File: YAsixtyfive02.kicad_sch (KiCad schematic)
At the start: 60 parts, among them J1 ~{NMI}, J2 Aux 5VDC, J3 Power 5V, J4 Expansion Bus, J7 GND, J8 FTDI Serial2USB, SW1 RESET, SW2 SW_Push_DPDT, U1 WD65C02, U10 74LS138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

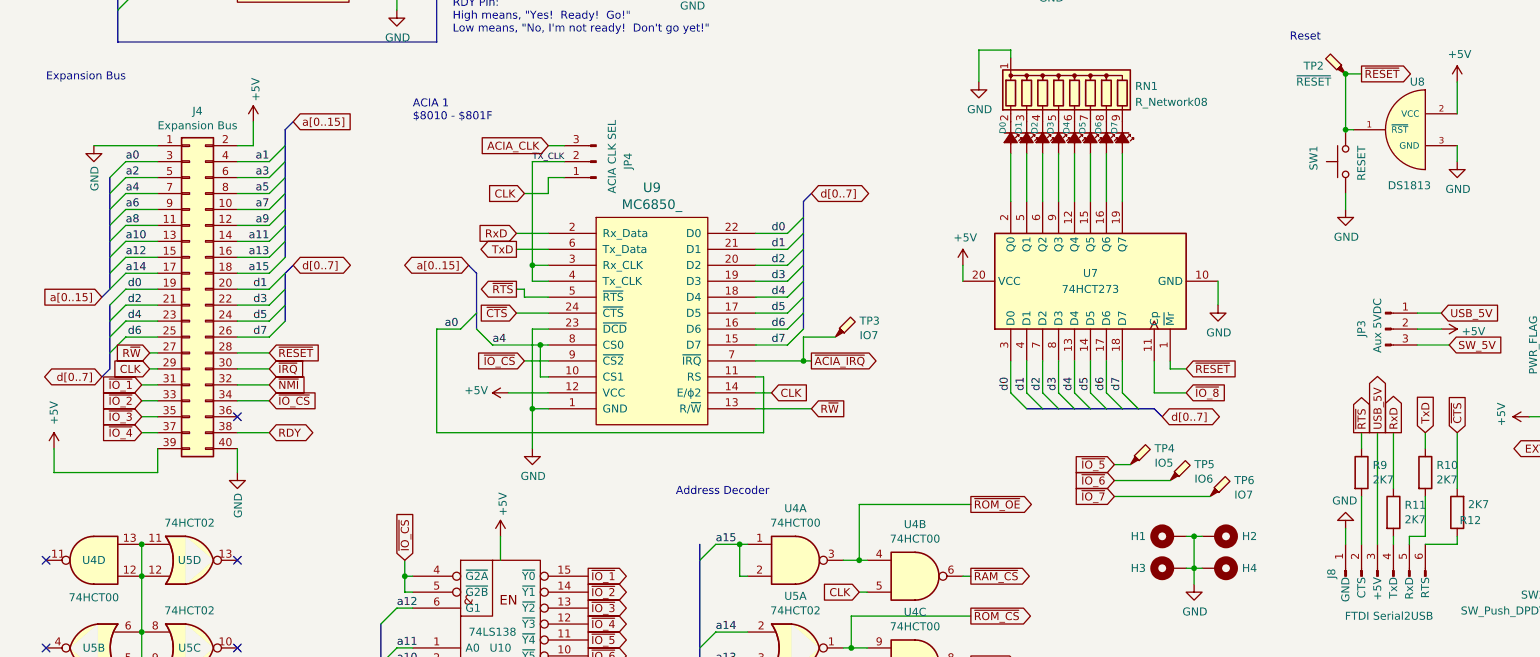
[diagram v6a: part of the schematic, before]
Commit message: PCB Almost ready missing USB Power override
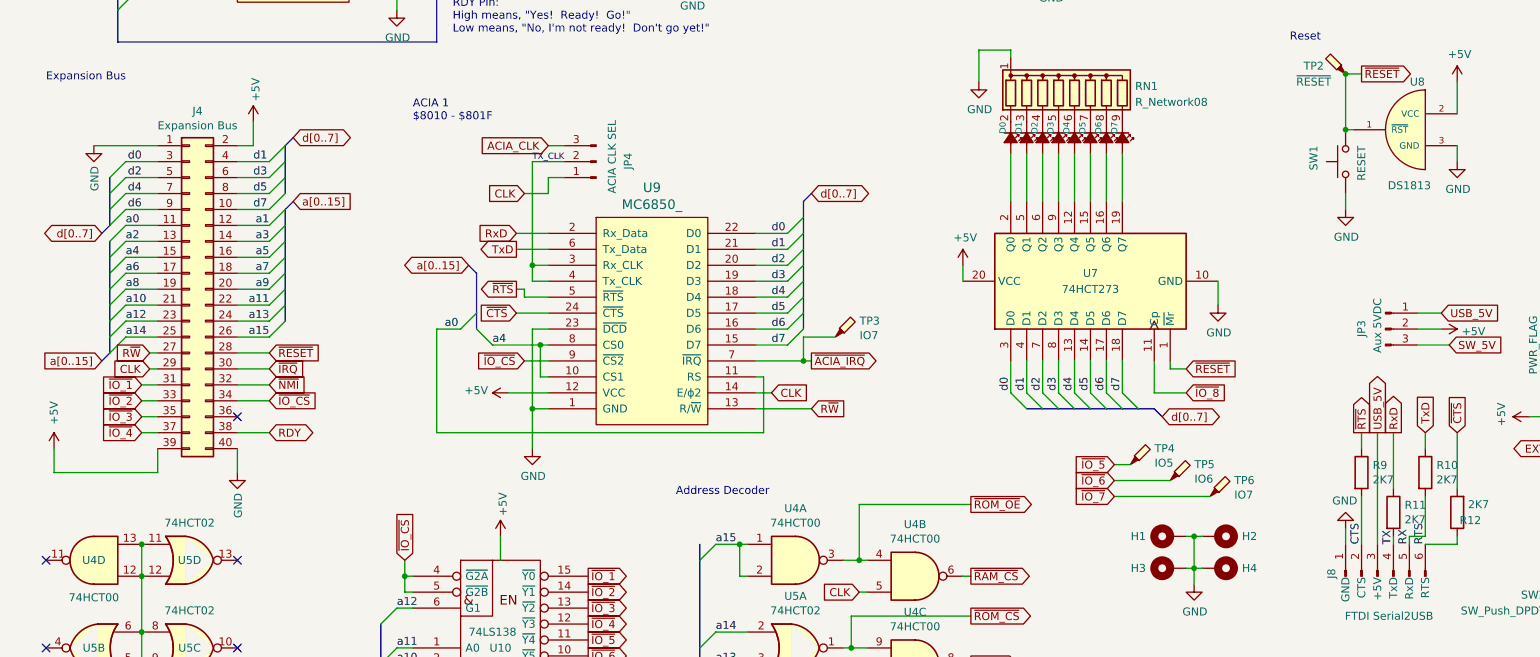
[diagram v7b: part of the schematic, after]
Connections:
- net a0: now also J4.11 (Pin_11); no longer J4.3 (Pin_3)
- net a1: now also J4.12 (Pin_12); no longer J4.4 (Pin_4)
- net a10: now also J4.21 (Pin_21); no longer J4.13 (Pin_13)
- net a11: now also J4.22 (Pin_22); no longer J4.14 (Pin_14)
- net a12: now also J4.23 (Pin_23); no longer J4.15 (Pin_15)
- net a13: now also J4.24 (Pin_24); no longer J4.16 (Pin_16)
- net a14: now also J4.25 (Pin_25); no longer J4.17 (Pin_17)
- net a15: now also J4.26 (Pin_26); no longer J4.18 (Pin_18)
- net a2: now also J4.13 (Pin_13); no longer J4.5 (Pin_5)
- net a3: now also J4.14 (Pin_14); no longer J4.6 (Pin_6)
- net a4: now also J4.15 (Pin_15); no longer J4.7 (Pin_7)
- net a5: now also J4.16 (Pin_16); no longer J4.8 (Pin_8)
- net a6: now also J4.17 (Pin_17); no longer J4.9 (Pin_9)
- net a7: now also J4.18 (Pin_18); no longer J4.10 (Pin_10)
- net a8: now also J4.19 (Pin_19); no longer J4.11 (Pin_11)
- net a9: now also J4.20 (Pin_20); no longer J4.12 (Pin_12)
- net d0: now also J4.3 (Pin_3); no longer J4.19 (Pin_19)
- net d1: now also J4.4 (Pin_4); no longer J4.20 (Pin_20)
- net d2: now also J4.5 (Pin_5); no longer J4.21 (Pin_21)
- net d3: now also J4.6 (Pin_6); no longer J4.22 (Pin_22)
- net d4: now also J4.7 (Pin_7); no longer J4.23 (Pin_23)
- net d5: now also J4.8 (Pin_8); no longer J4.24 (Pin_24)
- net d6: now also J4.9 (Pin_9); no longer J4.25 (Pin_25)
- net d7: now also J4.10 (Pin_10); no longer J4.26 (Pin_26)
- net CTS: now reaches J8.2 (CTS), R9.2
- net TX: now reaches J8.4 (TxD), R11.2
- net RX: now reaches J8.5 (RxD), R10.2
- net RTS: now reaches J8.6 (RTS), R12.1

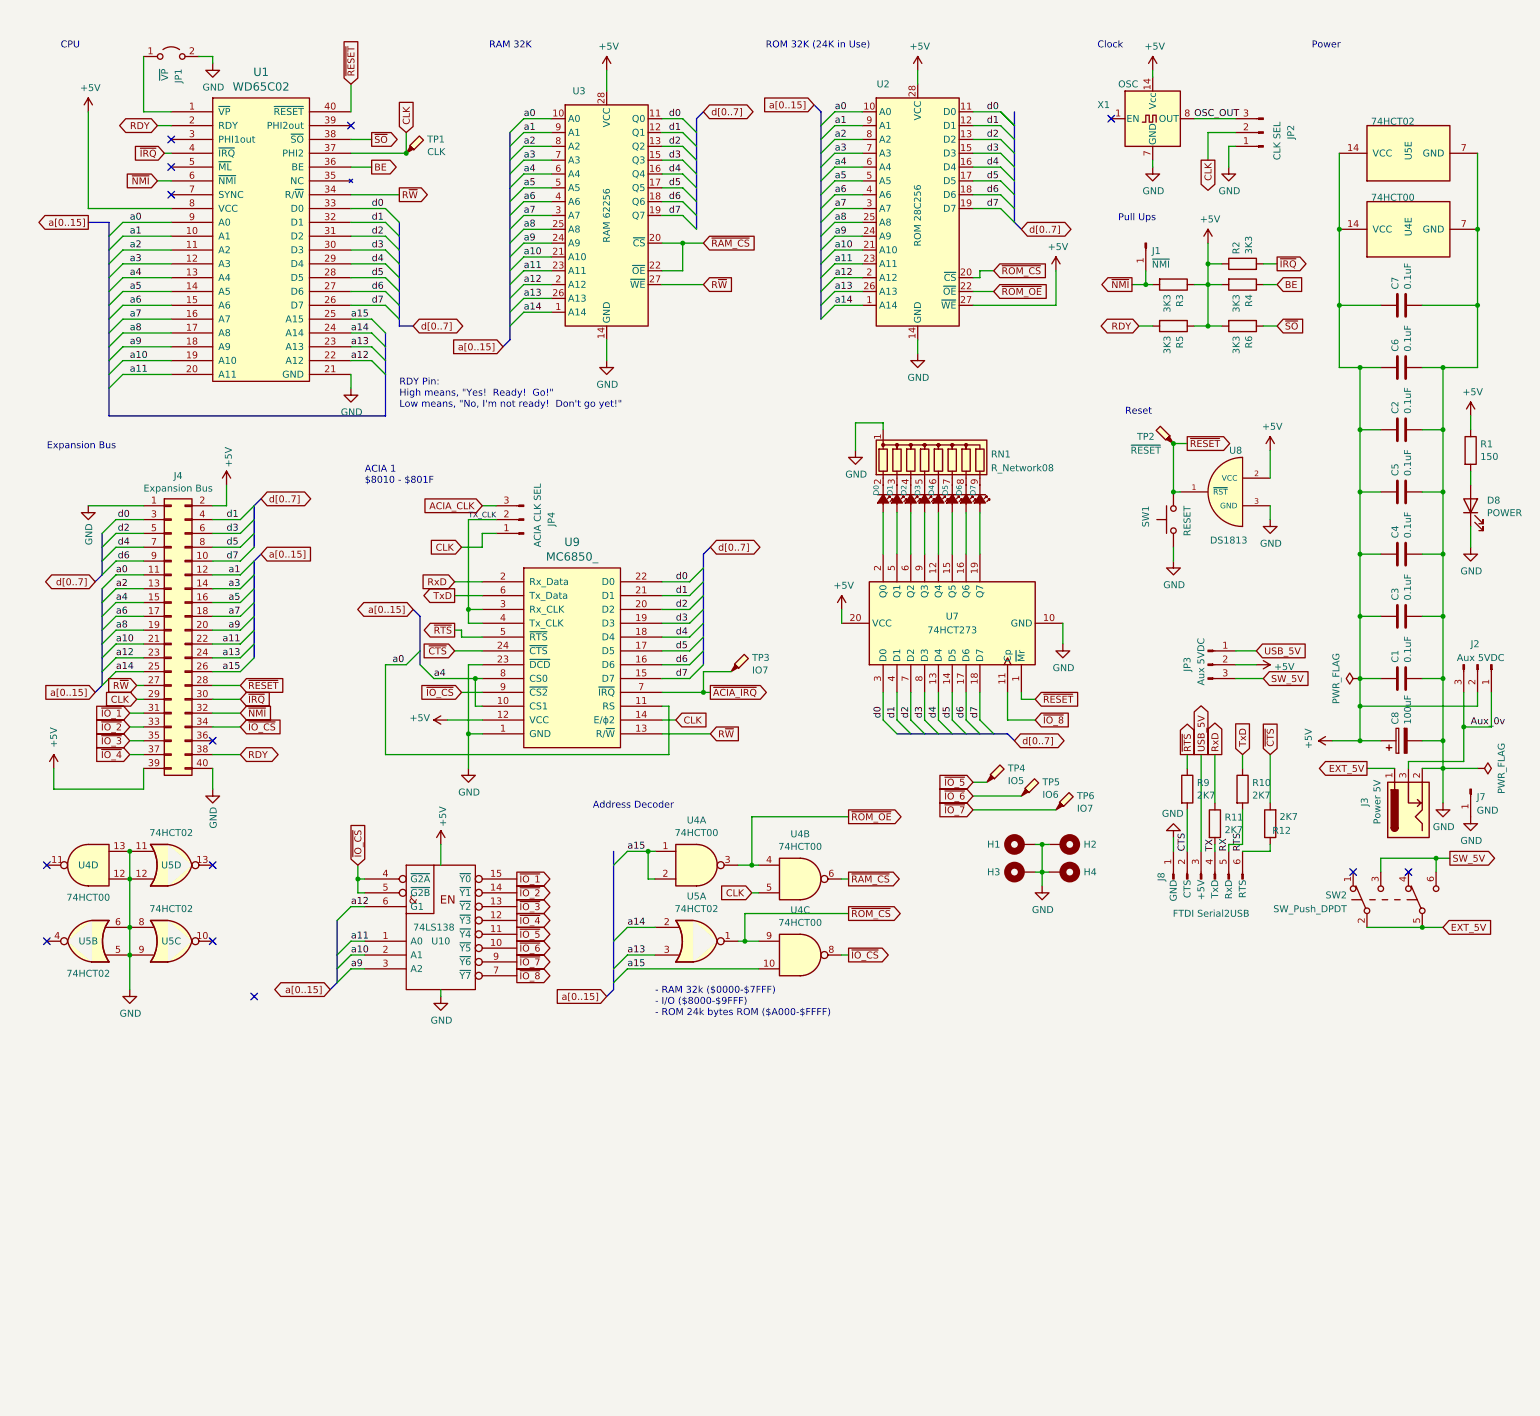
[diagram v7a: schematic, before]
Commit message: Updated to a more efficient memory map
Address Map
0x0000 - 0x7EFF : RAM (32K - 256 bytes)
0x7F00 - 0x7F0F : ACIA
0x7F10 - 0x7F1F : IO_2
0x7F20 - 0x7F2F : IO_3
0x7F30 - 0x7F7F : IO_4...IO_8
0x8000 - 0xFFFF : ROM (32K) << Should Bank this :)
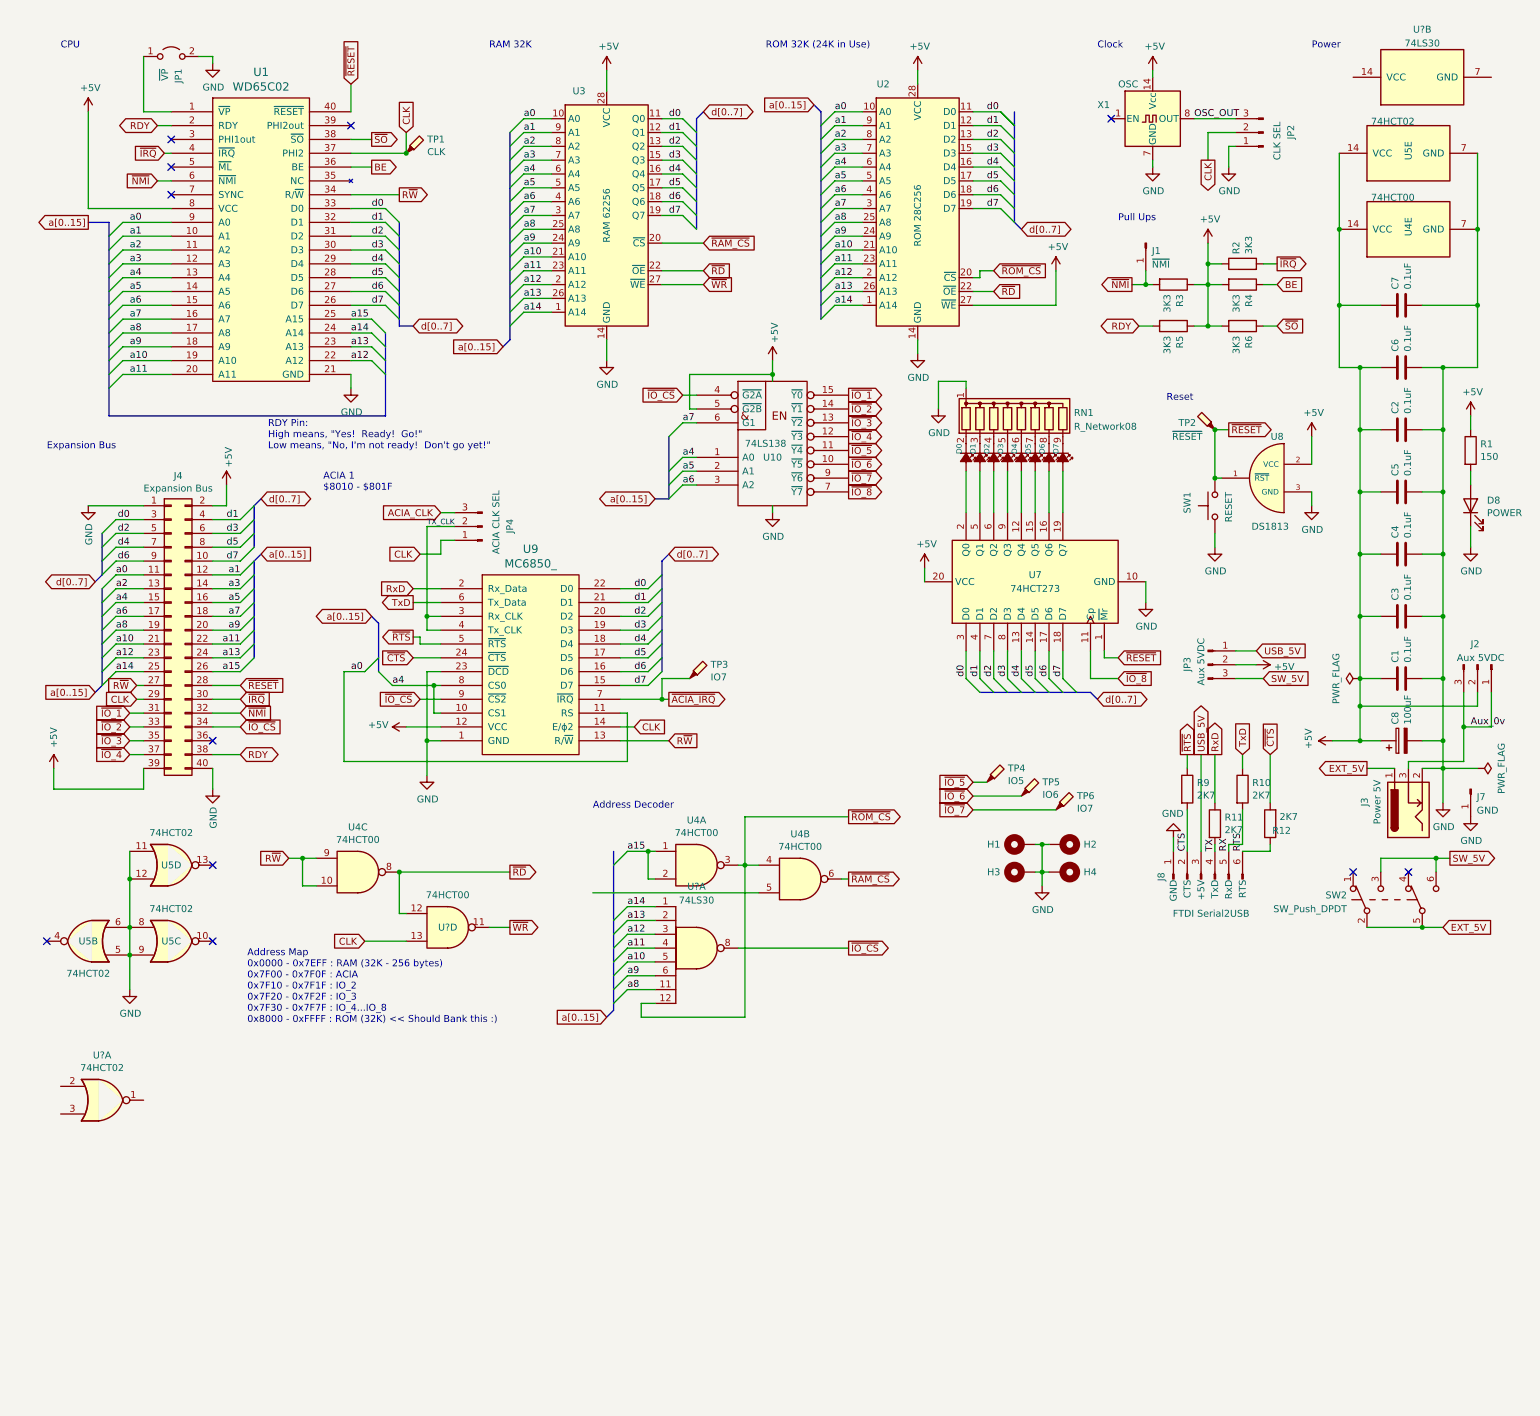
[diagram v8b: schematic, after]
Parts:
- removed unit 4 of U4
- removed unit 1 of U5
- added U? (x2): 74LS30, symbol 74xx:74LS30
- added U?: 74HCT02, Package_DIP:DIP-14_W7.62mm_Socket_LongPads, symbol 74xx:74HCT02
- added U?: 74HCT00, Package_DIP:DIP-14_W7.62mm_Socket_LongPads, symbol 74xx:74HCT00
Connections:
- net +5V: now also U10.5 (~{G2B})
- net CLK: now also U?.13; no longer U4.5
- net R~{W}: now also U4.10, U4.9; no longer U3.27 (~{WE})
- net a10: now also U?.5; no longer U10.2 (A1)
- net a11: now also U?.4; no longer U10.1 (A0)
- net a12: now also U?.3; no longer U10.6 (G1)
- net a13: now also U?.2
- net a14: now also U?.1
- net a15: no longer U4.10
- net a4: now also U10.1 (A0)
- net a5: now also U10.2 (A1)
- net a6: now also U10.3 (A2)
- net a7: now also U10.6 (G1)
- net a8: now also U?.11
- net a9: now also U?.6; no longer U10.3 (A2)
- net ~{IO_CS}: now also U?.8; no longer U10.5 (~{G2B}), U4.8
- net ~{RAM_CS}: no longer U3.22 (~{OE})
- net ~{ROM_CS}: now also U4.3, U4.4, U?.12; no longer U4.9
- removed net ~{ROM_OE}: U2.22 (~{OE}), U4.3, U4.4
- new net ~{RD}: U2.22 (~{OE}), U3.22 (~{OE}), U4.8, U?.12
- new net ~{WR}: U3.27 (~{WE}), U?.11
- no-connect marks 13 -> 11
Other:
- note added: "Address Map 0x0000 - 0x7EFF : RAM (32K - 256 bytes) 0x7F00 - 0x7F0F : ACIA 0x7F10 - 0x7F1F : IO_2 0x7F20 - 0x7F2F : IO_3 0x7F30 - 0x7F7F : IO_4...IO_8 0x8000 - 0xFFFF : ROM (32K) << Should Bank this :)"
- note removed: "- RAM 32k ($0000-$7FFF) - I/O ($8000-$9FFF) - ROM 24k bytes ROM ($A000-$FFFF)"
- moved on the sheet: D0, D1, D2, D3, D4, D5, D6, D7, JP4, RN1, SW1, TP2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
